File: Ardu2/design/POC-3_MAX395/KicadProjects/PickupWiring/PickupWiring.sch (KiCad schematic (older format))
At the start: 25 parts, among them P1 Neck_Pup_Sheild, P2 Bridge_Pup_Sheild, P3 Metal_Bridge_GND, P4 5-Pos Selector, P5 Output Jack, P6 HD15 Carvin to PyGuitar, SW1 SWITCH_SPDT, SW10 SWITCH_SPDT, SW2 SWITCH_SPDT, SW3 SWITCH_SPDT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

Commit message: created new PCB for 10PDT
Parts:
- gave numbers to parts that had none: 1
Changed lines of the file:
@@
 	4490 2180 5550 2180
 $Comp
-L CONN_01X01 P?
+L CONN_01X01 P7
 U 1 1 586FFEBA
 P 2790 3790
-F 0 "P?" H 2709 3569 50  0001 C CNN
+F 0 "P7" H 2709 3569 50  0001 C CNN
 F 1 "Componet_Bay_Shielding_GND" H 2790 3900 50  0000 C CNN
 F 2 "" H 2790 3790 50  0000 C CNN

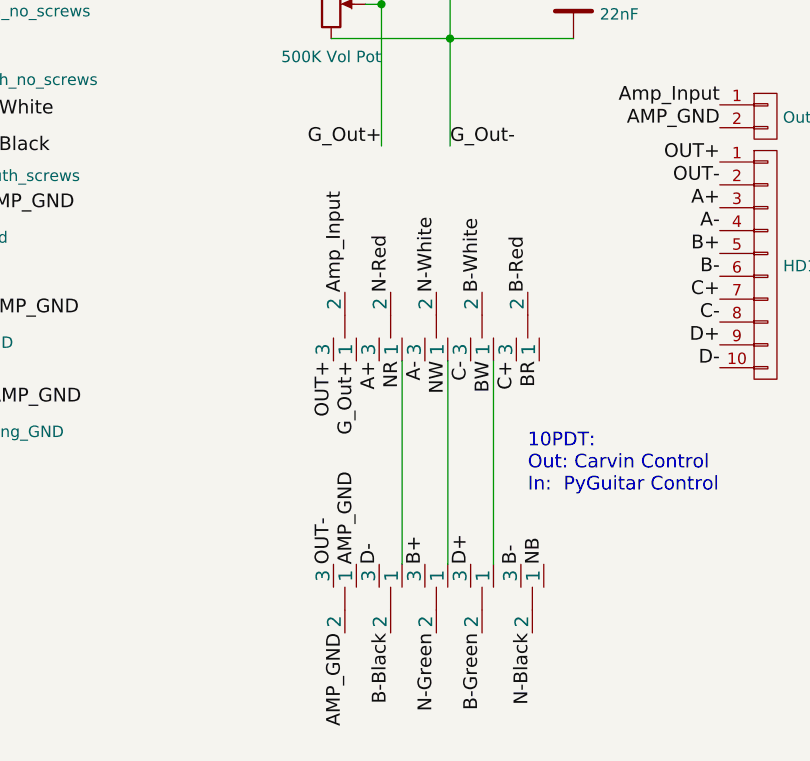
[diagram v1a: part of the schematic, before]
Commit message: updated guitar wiring
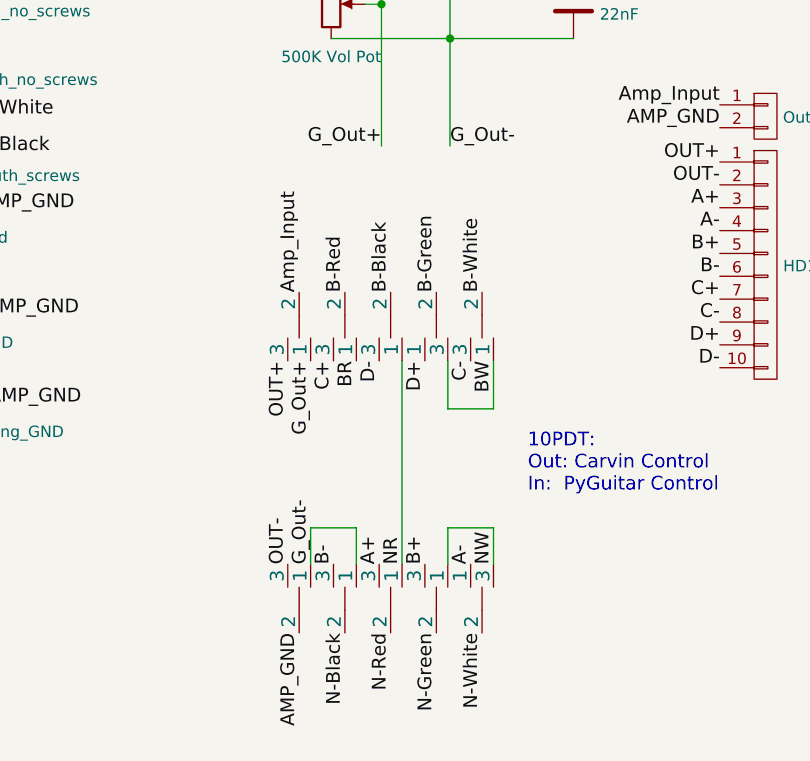
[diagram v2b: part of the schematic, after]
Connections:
- wire segments 13 -> 20
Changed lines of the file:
@@
 L SWITCH_SPDT SW7
 U 1 1 586FD7B8
-P 5350 3440
-F 0 "SW7" V 5350 3722 50  0001 C CNN
-F 1 "SWITCH_SPDT" H 5350 3633 50  0001 C CNN
-F 2 "" H 5350 3440 60  0000 C CNN
-F 3 "" H 5350 3440 60  0000 C CNN
-	1    5350 3440
+P 4550 3440
+F 0 "SW7" V 4550 3722 50  0001 C CNN
+F 1 "SWITCH_SPDT" H 4550 3633 50  0001 C CNN
+F 2 "" H 4550 3440 60  0000 C CNN
+F 3 "" H 4550 3440 60  0000 C CNN
+	1    4550 3440
 	0    1    1    0
 $EndComp
@@
 L SWITCH_SPDT SW5
 U 1 1 586FD7E1
+P 5150 4630
+F 0 "SW5" V 5150 4912 50  0001 C CNN
+F 1 "SWITCH_SPDT" H 5150 4823 50  0001 C CNN
+F 2 "" H 5150 4630 60  0000 C CNN
+F 3 "" H 5150 4630 60  0000 C CNN
+	1    5150 4630
+	0    -1   -1   0
+$EndComp
+$Comp
+L SWITCH_SPDT SW3
+U 1 1 586FD837
+P 4750 4630
+F 0 "SW3" V 4750 4912 50  0001 C CNN
+F 1 "SWITCH_SPDT" H 4750 4823 50  0001 C CNN
+F 2 "" H 4750 4630 60  0000 C CNN
+F 3 "" H 4750 4630 60  0000 C CNN
+	1    4750 4630
+	0    1    -1   0
+$EndComp
+$Comp
+L SWITCH_SPDT SW1
+U 1 1 586FD83D
+P 4350 3440
+F 0 "SW1" V 4350 3722 50  0001 C CNN
+F 1 "SWITCH_SPDT" H 4350 3633 50  0001 C CNN
+F 2 "" H 4350 3440 60  0000 C CNN
+F 3 "" H 4350 3440 60  0000 C CNN
+	1    4350 3440
+	0    1    1    0
+$EndComp
+$Comp
+L SWITCH_SPDT SW10
+U 1 1 586FD9BC
 P 4950 3440
-F 0 "SW5" V 4950 3722 50  0001 C CNN
+F 0 "SW10" V 4950 3722 50  0001 C CNN
 F 1 "SWITCH_SPDT" H 4950 3633 50  0001 C CNN
 F 2 "" H 4950 3440 60  0000 C CNN
 F 3 "" H 4950 3440 60  0000 C CNN
 	1    4950 3440
-	0    1    1    0
-$EndComp
-$Comp
-L SWITCH_SPDT SW3
-U 1 1 586FD837
+	0    -1   1    0
+$EndComp
+$Comp
+L SWITCH_SPDT SW8
+U 1 1 586FD9C2
 P 4750 3440
-F 0 "SW3" V 4750 3722 50  0001 C CNN
+F 0 "SW8" V 4750 3722 50  0001 C CNN
 F 1 "SWITCH_SPDT" H 4750 3633 50  0001 C CNN
 F 2 "" H 4750 3440 60  0000 C CNN
@@
 	1    4750 3440
 	0    1    1    0
-$EndComp
-$Comp
-L SWITCH_SPDT SW1
-U 1 1 586FD83D
-P 4550 3440
-F 0 "SW1" V 4550 3722 50  0001 C CNN
-F 1 "SWITCH_SPDT" H 4550 3633 50  0001 C CNN
-F 2 "" H 4550 3440 60  0000 C CNN
-F 3 "" H 4550 3440 60  0000 C CNN
-	1    4550 3440
-	0    1    1    0
-$EndComp
-$Comp
-L SWITCH_SPDT SW10
-U 1 1 586FD9BC
-P 5150 4630
-F 0 "SW10" V 5150 4912 50  0001 C CNN
-F 1 "SWITCH_SPDT" H 5150 4823 50  0001 C CNN
-F 2 "" H 5150 4630 60  0000 C CNN
-F 3 "" H 5150 4630 60  0000 C CNN
-	1    5150 4630
-	0    1    -1   0
-$EndComp
-$Comp
-L SWITCH_SPDT SW8
-U 1 1 586FD9C2
-P 4750 4630
-F 0 "SW8" V 4750 4912 50  0001 C CNN
-F 1 "SWITCH_SPDT" H 4750 4823 50  0001 C CNN
-F 2 "" H 4750 4630 60  0000 C CNN
-F 3 "" H 4750 4630 60  0000 C CNN
-	1    4750 4630
-	0    1    -1   0
 $EndComp
 $Comp
@@
 L SWITCH_SPDT SW4
 U 1 1 586FD9CE
-P 5370 4630
-F 0 "SW4" V 5370 4912 50  0001 C CNN
-F 1 "SWITCH_SPDT" H 5370 4823 50  0001 C CNN
-F 2 "" H 5370 4630 60  0000 C CNN
-F 3 "" H 5370 4630 60  0000 C CNN
-	1    5370 4630
-	0    1    -1   0
-$EndComp
-$Comp
-L SWITCH_SPDT SW2
-U 1 1 586FD9D4
 P 4550 4630
-F 0 "SW2" V 4550 4912 50  0001 C CNN
+F 0 "SW4" V 4550 4912 50  0001 C CNN
 F 1 "SWITCH_SPDT" H 4550 4823 50  0001 C CNN
 F 2 "" H 4550 4630 60  0000 C CNN
 F 3 "" H 4550 4630 60  0000 C CNN
 	1    4550 4630
+	0    1    -1   0
+$EndComp
+$Comp
+L SWITCH_SPDT SW2
+U 1 1 586FD9D4
+P 4350 4630
+F 0 "SW2" V 4350 4912 50  0001 C CNN
+F 1 "SWITCH_SPDT" H 4350 4823 50  0001 C CNN
+F 2 "" H 4350 4630 60  0000 C CNN
+F 3 "" H 4350 4630 60  0000 C CNN
+	1    4350 4630
 	0    1    -1   0
 $EndComp
@@
 Text Notes 5350 4170 0    60   ~ 0
 10PDT:\nOut: Carvin Control\nIn:  PyGuitar Control
-Text Label 4750 3290 1    60   ~ 0
+Text Label 4750 4780 3    60   ~ 0
 N-Red
-Text Label 4950 3290 1    60   ~ 0
+Text Label 5150 4780 3    60   ~ 0
 N-White
 Text Label 4950 4780 3    60   ~ 0
 N-Green
-Text Label 5370 4780 3    60   ~ 0
+Text Label 4550 4780 3    60   ~ 0
 N-Black
+Text Label 4350 3290 1    60   ~ 0
+Amp_Input
+Text Label 4350 4780 3    60   ~ 0
+AMP_GND
+Text Label 4750 3290 1    60   ~ 0
+B-Black
+Text Label 4950 3290 1    60   ~ 0
+B-Green
 Text Label 4550 3290 1    60   ~ 0
-Amp_Input
-Text Label 4550 4780 3    60   ~ 0
-AMP_GND
-Text Label 4750 4780 3    60   ~ 0
-B-Black
-Text Label 5150 4780 3    60   ~ 0
-B-Green
-Text Label 5350 3290 1    60   ~ 0
 B-Red
 Text Label 5150 3290 1    60   ~ 0
 B-White
-Text Label 4600 3590 3    60   ~ 0
+Text Label 4400 3590 3    60   ~ 0
 G_Out+
-Text Label 4600 4480 1    60   ~ 0
-AMP_GND
 $Comp
 L CONN_01X01 P3
@@
 Text Label 6190 3620 2    60   ~ 0
 D-
-Text Label 4800 3590 3    60   ~ 0
+Text Label 4800 4480 1    60   ~ 0
 NR
-Text Label 4700 3590 3    60   ~ 0
+Text Label 4700 4480 1    60   ~ 0
 A+
-Text Label 4500 3590 3    60   ~ 0
+Text Label 4300 3590 3    60   ~ 0
 OUT+
-Text Label 4900 3590 3    60   ~ 0
+Text Label 5100 4480 1    60   ~ 0
 A-
-Text Label 5320 4480 1    60   ~ 0
+Text Label 4500 4480 1    60   ~ 0
 B-
 Text Label 4900 4480 1    60   ~ 0
 B+
-Text Label 5300 3590 3    60   ~ 0
+Text Label 4500 3590 3    60   ~ 0
 C+
 Text Label 5100 3590 3    60   ~ 0
 C-
-Text Label 5100 4480 1    60   ~ 0
+Text Label 4900 3590 3    60   ~ 0
 D+
-Text Label 4700 4480 1    60   ~ 0
-D-
-Text Label 4500 4480 1    60   ~ 0
+Text Label 4300 4480 1    60   ~ 0
 OUT-
 NoConn ~ 5210 1340
 NoConn ~ 4510 1340
-Text Label 5400 3590 3    60   ~ 0
+Text Label 4600 3590 3    60   ~ 0
 BR
 Text Label 5200 3590 3    60   ~ 0
 BW
-Text Label 5420 4480 1    60   ~ 0
-NB
-Text Label 5000 3590 3    60   ~ 0
+Text Label 5200 4480 1    60   ~ 0
 NW
 $Comp
@@
 	4810 1340 4910 1340
 Wire Wire Line
-	5000 3590 5000 4480
-Wire Wire Line
-	5200 4480 5200 3590
-Wire Wire Line
-	4800 3590 4800 4480
+	4800 4480 4800 3590
 Connection ~ 4710 1730
 Wire Wire Line
@@
 Text Notes 4730 1140 2    30   ~ 0
 4 3 2 1 0
+Text Label 4400 4480 1    60   ~ 0
+G_Out-
+Wire Wire Line
+	4600 4480 4600 4320
+Wire Wire Line
+	4600 4320 4400 4320
+Wire Wire Line
+	4400 4320 4400 4480
+Wire Wire Line
+	5000 4480 5000 4320
+Wire Wire Line
+	5000 4320 5200 4320
+Wire Wire Line
+	5200 4320 5200 4480
+Text Label 4700 3590 3    60   ~ 0
+D-
+Wire Wire Line
+	5000 3590 5000 3800
+Wire Wire Line
+	5000 3800 5200 3800
+Wire Wire Line
+	5200 3800 5200 3590
 $EndSCHEMATC
